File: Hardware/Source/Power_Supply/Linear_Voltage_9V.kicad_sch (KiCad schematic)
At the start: 23 parts, among them U7 TPS54331DR, U8 L7809CV

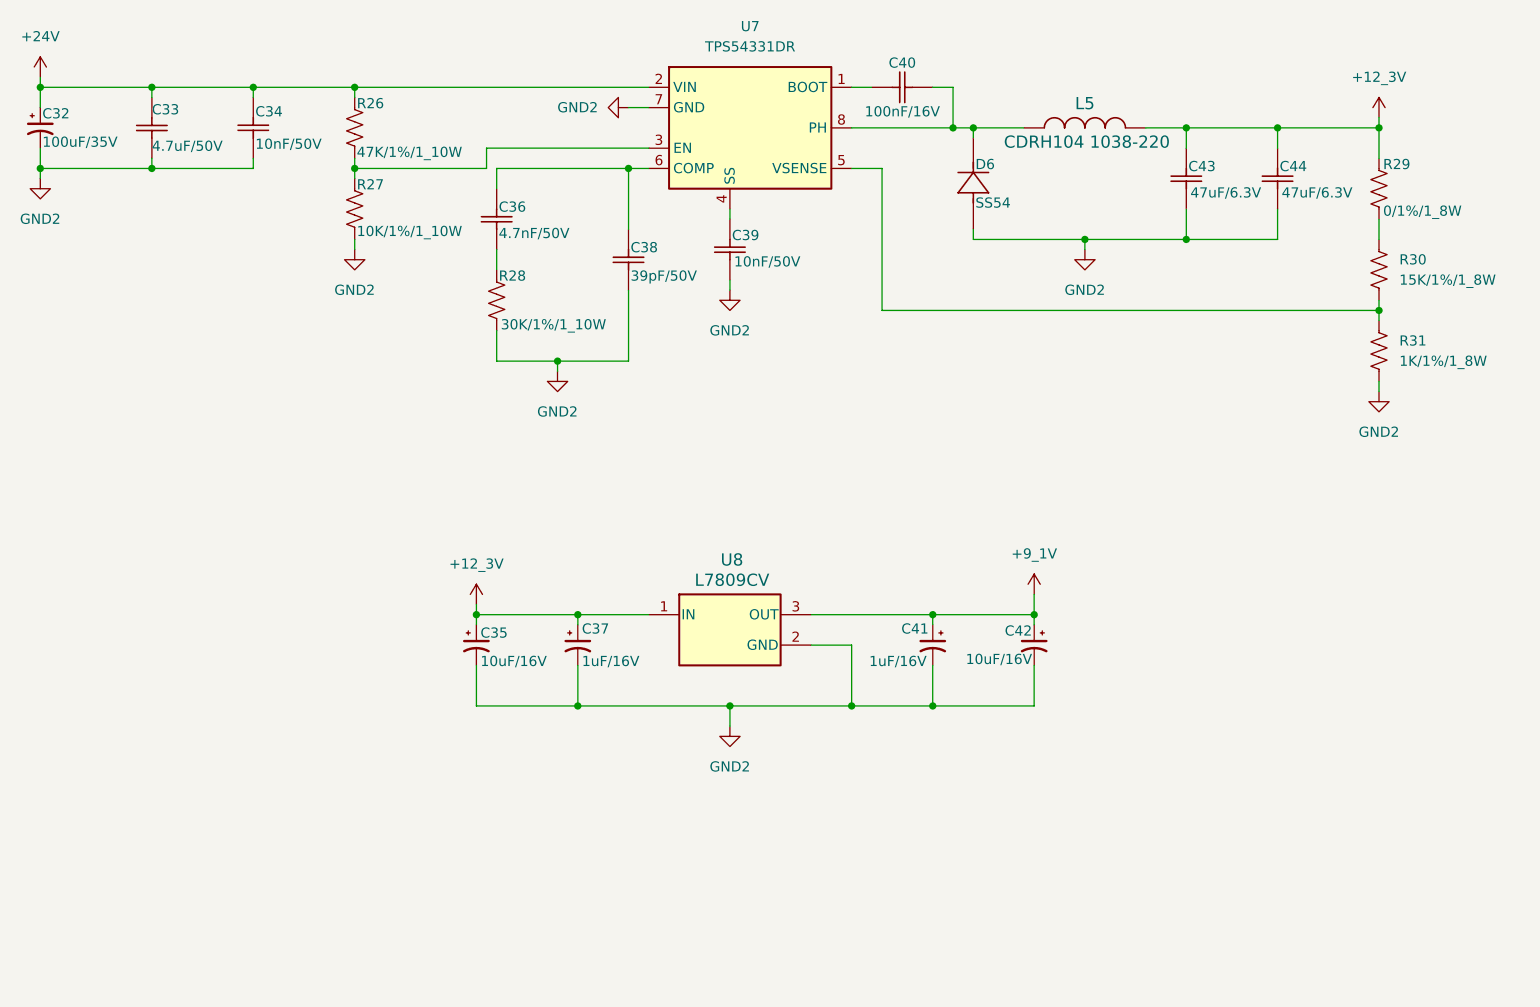
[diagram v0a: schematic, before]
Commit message: update new flyback lib
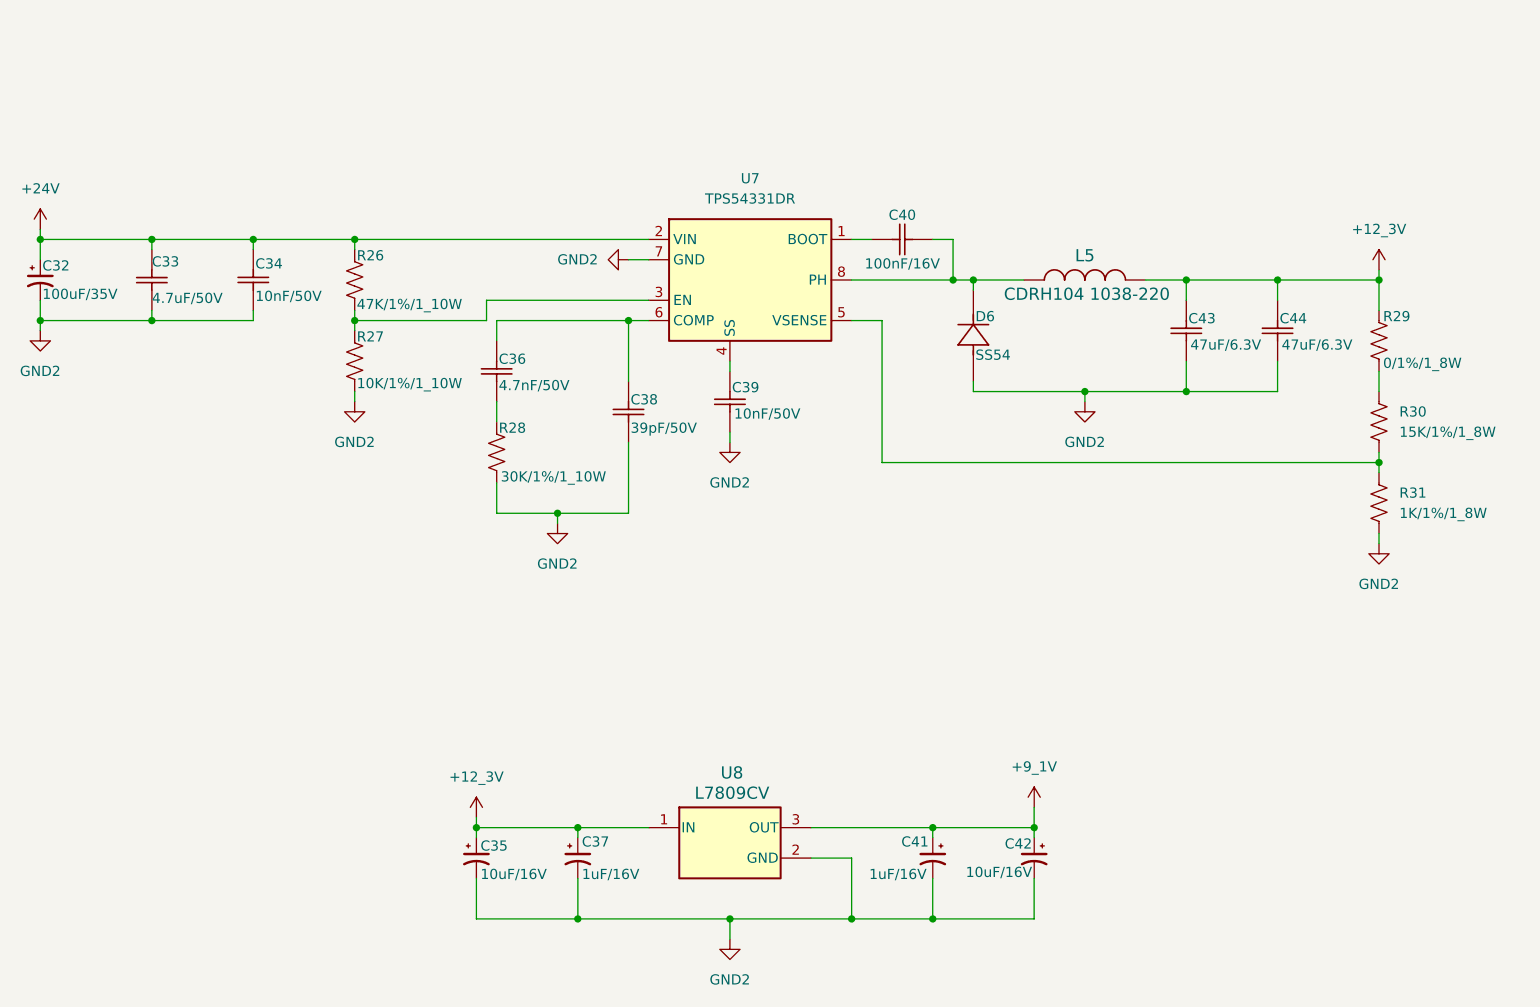
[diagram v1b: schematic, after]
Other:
- moved on the sheet: C32, C33, C34, C35, C36, C37, C38, C39, C40, C41, C42, C43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

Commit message: update
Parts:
- removed C32: 100uF/35V, Capacitor_SMD:CP_Elec_5x5.4, symbol charge_battery_sym_lib:Cap_Polarized_SMD_100uF_35V
- removed C33: 4.7uF/50V, charge_battery_footprint_lib:Ceramic_Cap_0805, symbol charge_battery_sym_lib:Ceramic_Cap_SMD_4.7uF_50V
- removed C34: 10nF/50V, charge_battery_footprint_lib:Ceramic_Cap_0805, symbol charge_battery_sym_lib:Ceramic_Cap_SMD_10nF_50V_0805
- removed C36: 4.7nF/50V, charge_battery_footprint_lib:Ceramic_Cap_0603, symbol charge_battery_sym_lib:Ceramic_Cap_SMD_4.7nF_50V
- removed C38: 39pF/50V, charge_battery_footprint_lib:Ceramic_Cap_0603, symbol charge_battery_sym_lib:Ceramic_Cap_SMD_39pF_50V
- removed C39: 10nF/50V, charge_battery_footprint_lib:Ceramic_Cap_0603, symbol charge_battery_sym_lib:Ceramic_Cap_SMD_10nF_50V
- removed C40: 100nF/16V, charge_battery_footprint_lib:Ceramic_Cap_0603, symbol charge_battery_sym_lib:Ceramic_Cap_SMD_100nF_16V
- removed C43, C44: 47uF/6.3V, charge_battery_footprint_lib:Ceramic_Cap_0805, symbol charge_battery_sym_lib:Ceramic_Cap_SMD_47uF_6.3V
- removed D6: SS54, charge_battery_footprint_lib:D_SMA, symbol charge_battery_sym_lib:SS54
- removed L5: CDRH104 1038-220, charge_battery_footprint_lib:CDRH104, symbol charge_battery_sym_lib:CDRH104 1038-220
- removed R26: 47K/1%/1_10W, charge_battery_footprint_lib:Res_0603, symbol charge_battery_sym_lib:Res_47K_0603_1%
- removed R27: 10K/1%/1_10W, charge_battery_footprint_lib:Res_0603, symbol charge_battery_sym_lib:Res_10K_0603_1%
- removed R28: 30K/1%/1_10W, charge_battery_footprint_lib:Res_0603, symbol charge_battery_sym_lib:Res_30K_0603_1%
- removed R29: 0/1%/1_8W, charge_battery_footprint_lib:Res_0805, symbol charge_battery_sym_lib:Res_0_0805_1%
- removed R30: 15K/1%/1_8W, charge_battery_footprint_lib:Res_0805, symbol charge_battery_sym_lib:Res_15K_0805_1%
- removed R31: 1K/1%/1_8W, charge_battery_footprint_lib:Res_0805, symbol charge_battery_sym_lib:Res_1K_0805_1%
- removed U7: TPS54331DR, charge_battery_footprint_lib:SOIC-8, symbol charge_battery_sym_lib:TPS54331DR
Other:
- moved on the sheet: C35, C37, C41, C42, U8

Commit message: update lib PSC
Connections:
- net +12_3V renamed +12V
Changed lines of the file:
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@@
 		(on_board yes)
 		(dnp no)
-		(fields_autoplaced yes)
 		(property "Reference" "#PWR030"
 			(at 168.91 80.01 0)
@@
 		)
 		(property "Value" "+9_1V"
-			(at 168.91 71.12 0)
+			(at 168.656 72.644 0)
 			(effects
 				(font
@@
 		(on_board yes)
 		(dnp no)
-		(fields_autoplaced yes)
 		(property "Reference" "#PWR025"
 			(at 99.06 81.28 0)
@@
 			)
 		)
-		(property "Value" "+12_3V"
-			(at 99.06 72.39 0)
+		(property "Value" "+12V"
+			(at 96.266 73.66 0)
 			(effects
 				(font
 					(size 1.27 1.27)
 				)
+				(justify left)
 			)
 		)

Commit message: Update Lib PSC
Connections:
- net +9_1V renamed +9
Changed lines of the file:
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@@
 			)
 		)
-		(property "Value" "+9_1V"
+		(property "Value" "+9"
 			(at 168.656 72.644 0)
 			(effects

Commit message: Update Lib ER35 Transformer
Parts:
- renumbered C35 to C17, C37 to C18, C41 to C19, C42 to C20, U8 to U5
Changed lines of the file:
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@@
 		(on_board yes)
 		(dnp no)
-		(property "Reference" "C42"
+		(property "Reference" "C20"
 			(at 168.656 80.772 90)
 			(effects
@@
 			(project "Power_Supply"
 				(path "/5c8a7907-026b-4416-b231-5ef9f93b99e1/409c1703-669f-4885-84ed-c53b20e63f53"
-					(reference "C42")
+					(reference "C20")
 					(unit 1)
 				)
@@
 		(on_board yes)
 		(dnp no)
-		(property "Reference" "C41"
+		(property "Reference" "C19"
 			(at 155.702 80.518 90)
 			(effects
@@
 			(project "Power_Supply"
 				(path "/5c8a7907-026b-4416-b231-5ef9f93b99e1/409c1703-669f-4885-84ed-c53b20e63f53"
-					(reference "C41")
+					(reference "C19")
 					(unit 1)
 				)
@@
 		(on_board yes)
 		(dnp no)
-		(property "Reference" "C35"
+		(property "Reference" "C17"
 			(at 99.568 81.026 90)
 			(effects
@@
 			(project "Power_Supply"
 				(path "/5c8a7907-026b-4416-b231-5ef9f93b99e1/409c1703-669f-4885-84ed-c53b20e63f53"
-					(reference "C35")
+					(reference "C17")
 					(unit 1)
 				)
@@
 		(on_board yes)
 		(dnp no)
-		(property "Reference" "#PWR030"
+		(property "Reference" "#PWR07"
 			(at 168.91 80.01 0)
 			(effects
@@
 			(project "Power_Supply"
 				(path "/5c8a7907-026b-4416-b231-5ef9f93b99e1/409c1703-669f-4885-84ed-c53b20e63f53"
-					(reference "#PWR030")
+					(reference "#PWR07")
 					(unit 1)
 				)
@@
 		(on_board yes)
 		(dnp no)
-		(property "Reference" "C37"
+		(property "Reference" "C18"
 			(at 112.268 80.518 90)
 			(effects
@@
 			(project "Power_Supply"
 				(path "/5c8a7907-026b-4416-b231-5ef9f93b99e1/409c1703-669f-4885-84ed-c53b20e63f53"
-					(reference "C37")
+					(reference "C18")
 					(unit 1)
 				)
@@
 		(on_board yes)
 		(dnp no)
-		(property "Reference" "#PWR025"
+		(property "Reference" "#PWR05"
 			(at 99.06 81.28 0)
 			(effects
@@
 			(project "Power_Supply"
 				(path "/5c8a7907-026b-4416-b231-5ef9f93b99e1/409c1703-669f-4885-84ed-c53b20e63f53"
-					(reference "#PWR025")
+					(reference "#PWR05")
 					(unit 1)
 				)
@@
 		(on_board yes)
 		(dnp no)
-		(property "Reference" "U8"
+		(property "Reference" "U5"
 			(at 131.064 71.882 0)
 			(effects
@@
 			(project "Power_Supply"
 				(path "/5c8a7907-026b-4416-b231-5ef9f93b99e1/409c1703-669f-4885-84ed-c53b20e63f53"
-					(reference "U8")
+					(reference "U5")
 					(unit 1)
 				)
@@
 		(dnp no)
 		(fields_autoplaced yes)
-		(property "Reference" "#PWR029"
+		(property "Reference" "#PWR06"
 			(at 130.81 99.06 0)
 			(effects
@@
 			(project "Power_Supply"
 				(path "/5c8a7907-026b-4416-b231-5ef9f93b99e1/409c1703-669f-4885-84ed-c53b20e63f53"
-					(reference "#PWR029")
-					(unit 1)
-				)
+					(reference "#PWR06")
+					(unit 1)
+				)
